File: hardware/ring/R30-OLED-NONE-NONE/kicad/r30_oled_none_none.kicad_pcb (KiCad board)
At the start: 2 copper layers, 43 x 18 mm, 28 parts, among them J1 off-board USB service pads, Q1 VBUS service jumper, SW1 5mm 200gf dome, U1 ESP32-C3-MINI-1-N4, U2 PAW3204DB-TJ3L, U3 TP4054, U4 RT9080-33GJ5

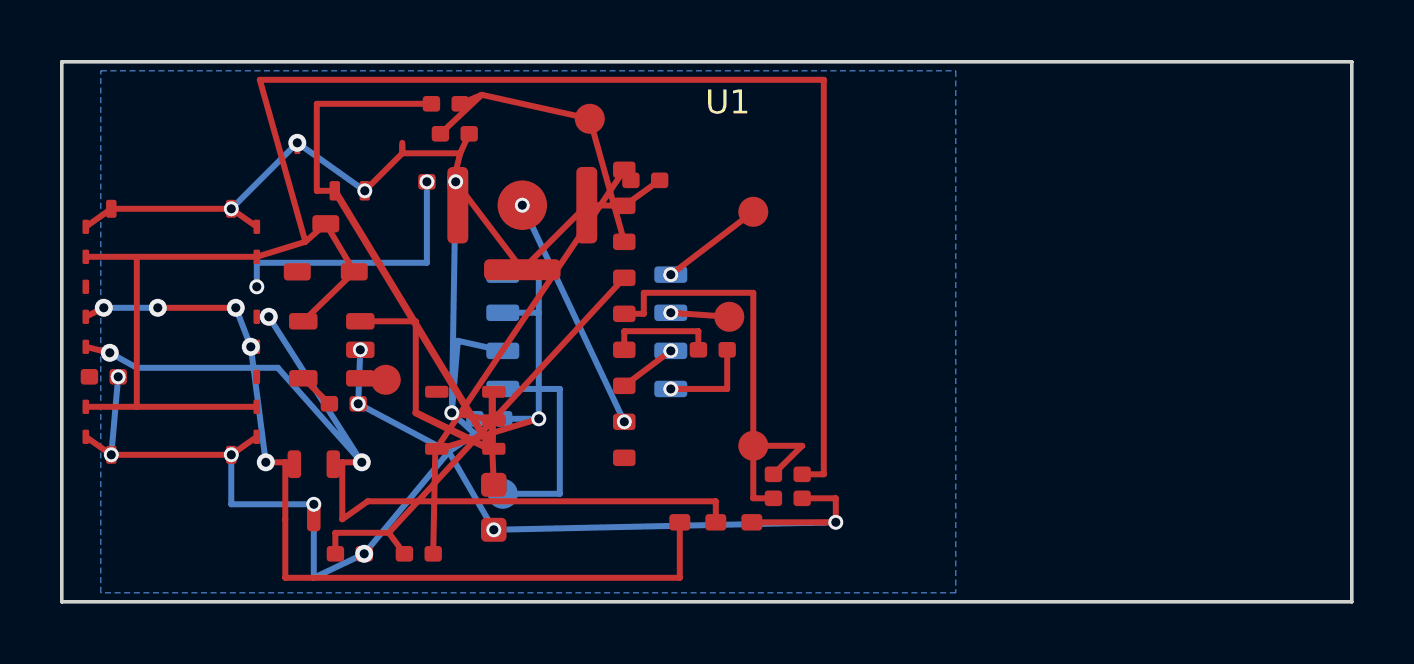
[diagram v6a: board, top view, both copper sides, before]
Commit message: fix(r30): nudge mcu decoupler clearance
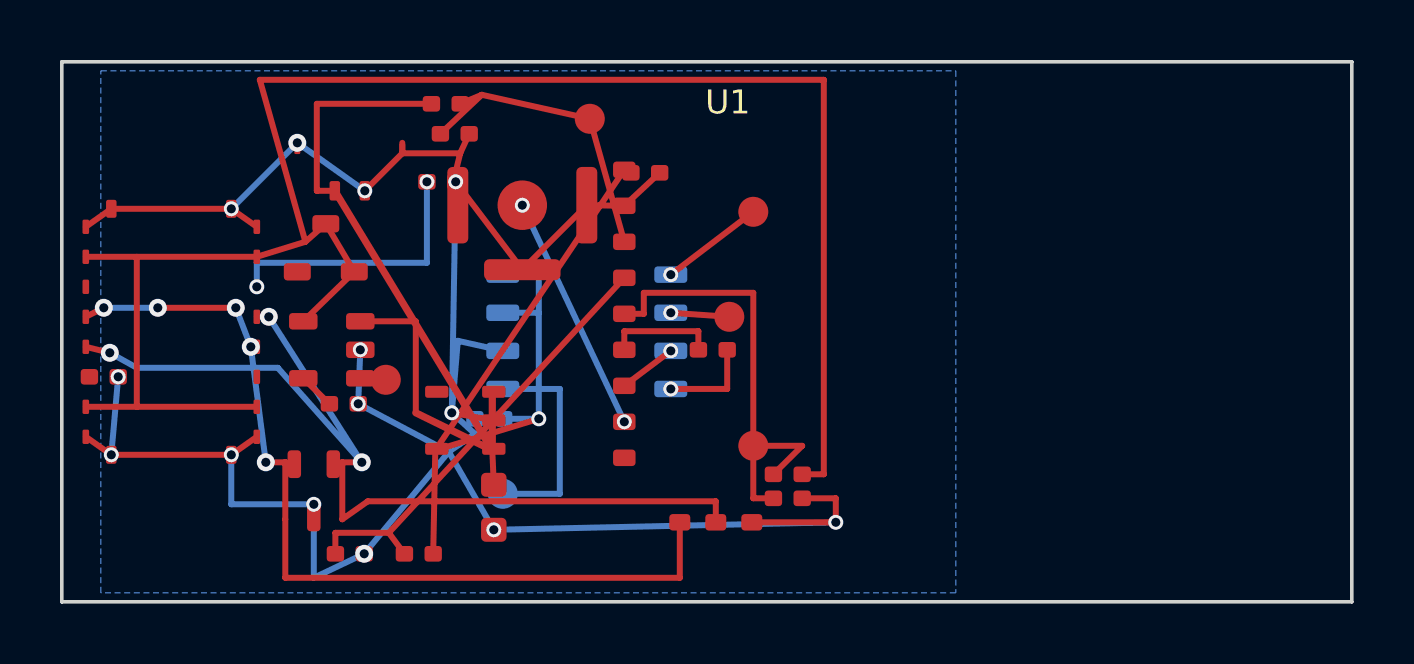
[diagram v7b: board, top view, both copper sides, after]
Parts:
- moved C1A 0.25 mm to (118.5, 94.7)
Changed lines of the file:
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@@
   (footprint "Capacitor_SMD:C_0402_1005Metric"
     (layer "F.Cu")
-    (at 118.450 94.950 0)
+    (at 118.450 94.700 0)
     (property "Reference" "C1A" (at 0 -1.05 0) (layer "F.Fab") (effects (font (size 0.6 0.6) (thickness 0.09))))
     (property "Value" "100nF MCU" (at 0 1.05 0) (layer "F.Fab") (effects (font (size 0.55 0.55) (thickness 0.08))))
@@
   (segment (start 113.350 103.950) (end 113.350 102.050) (width 0.24) (layer "F.Cu") (net 4))
   (segment (start 111.450 103.950) (end 117.750 94.600) (width 0.20) (layer "F.Cu") (net 5))
-  (segment (start 117.750 94.600) (end 117.970 94.950) (width 0.24) (layer "F.Cu") (net 5))
+  (segment (start 117.750 94.600) (end 117.970 94.700) (width 0.24) (layer "F.Cu") (net 5))
   (segment (start 111.450 103.950) (end 111.380 107.400) (width 0.20) (layer "F.Cu") (net 5))
   (segment (start 111.450 103.950) (end 114.900 102.900) (width 0.20) (layer "F.Cu") (net 5))
@@
   (segment (start 124.800 105.550) (end 124.800 106.350) (width 0.20) (layer "F.Cu") (net 1))
   (segment (start 124.800 106.350) (end 122.000 106.350) (width 0.20) (layer "F.Cu") (net 1))
-  (segment (start 118.930 94.950) (end 117.750 95.800) (width 0.20) (layer "F.Cu") (net 1))
+  (segment (start 118.930 94.700) (end 117.750 95.800) (width 0.20) (layer "F.Cu") (net 1))
   (segment (start 116.500 95.780) (end 117.750 95.800) (width 0.20) (layer "F.Cu") (net 1))
   (segment (start 108.120 107.400) (end 108.120 106.700) (width 0.20) (layer "F.Cu") (net 9))

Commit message: fix(r30): reroute vbat sense support corridor
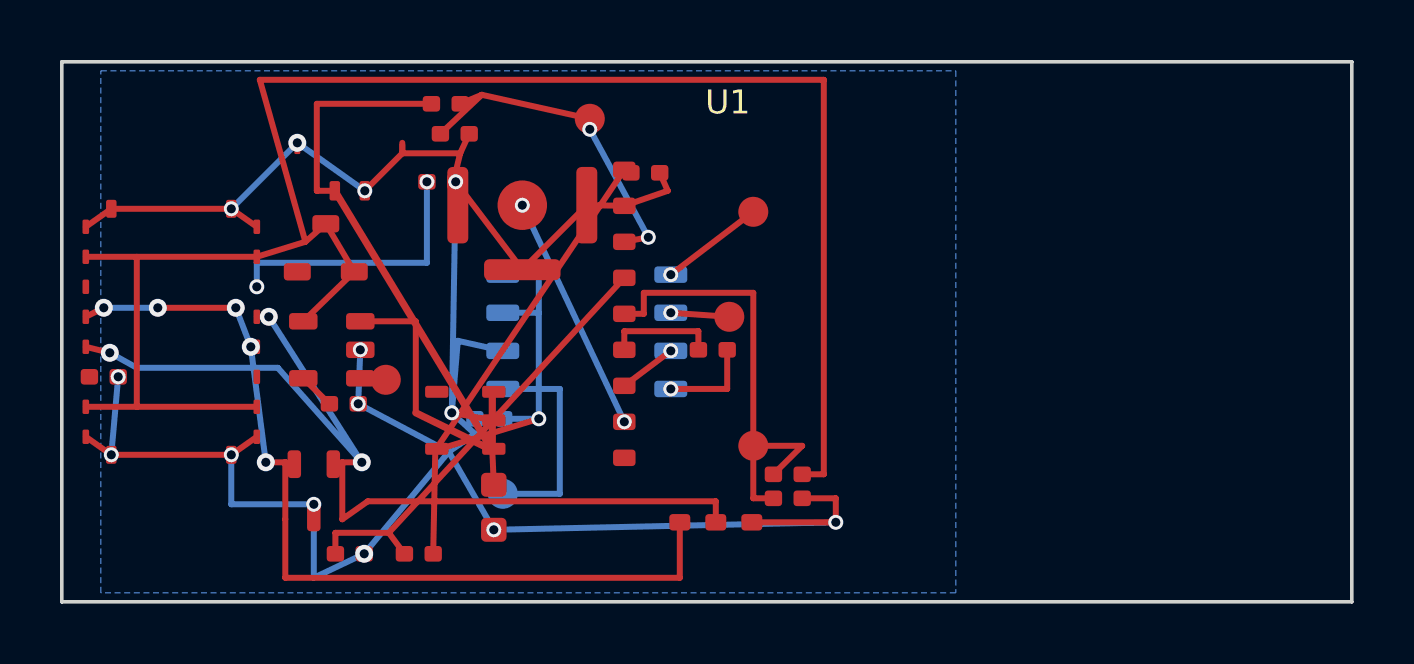
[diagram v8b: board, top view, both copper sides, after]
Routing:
- net VBAT_SENSE: track 10.6 -> 11.6 mm, vias 0 -> 2
- net GND: track 89.1 -> 89.7 mm
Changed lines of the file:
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@@
   (segment (start 124.800 105.550) (end 124.800 106.350) (width 0.20) (layer "F.Cu") (net 1))
   (segment (start 124.800 106.350) (end 122.000 106.350) (width 0.20) (layer "F.Cu") (net 1))
-  (segment (start 118.930 94.700) (end 117.750 95.800) (width 0.20) (layer "F.Cu") (net 1))
+  (segment (start 118.930 94.700) (end 119.200 95.300) (width 0.20) (layer "F.Cu") (net 1))
+  (segment (start 119.200 95.300) (end 117.750 95.800) (width 0.20) (layer "F.Cu") (net 1))
   (segment (start 116.500 95.780) (end 117.750 95.800) (width 0.20) (layer "F.Cu") (net 1))
   (segment (start 108.120 107.400) (end 108.120 106.700) (width 0.20) (layer "F.Cu") (net 9))
@@
   (segment (start 111.620 93.400) (end 113.000 92.100) (width 0.20) (layer "F.Cu") (net 21))
   (segment (start 113.000 92.100) (end 116.600 92.900) (width 0.20) (layer "F.Cu") (net 21))
-  (segment (start 116.600 92.900) (end 117.750 97.000) (width 0.20) (layer "F.Cu") (net 21))
+  (segment (start 116.600 92.900) (end 116.600 93.250) (width 0.20) (layer "F.Cu") (net 21))
+  (via (at 116.600 93.250) (size 0.50) (drill 0.30) (layers "F.Cu" "B.Cu") (net 21))
+  (segment (start 116.600 93.250) (end 118.550 96.850) (width 0.20) (layer "B.Cu") (net 21))
+  (via (at 118.550 96.850) (size 0.50) (drill 0.30) (layers "F.Cu" "B.Cu") (net 21))
+  (segment (start 118.550 96.850) (end 117.750 97.000) (width 0.20) (layer "F.Cu") (net 21))
   (segment (start 117.750 99.400) (end 118.400 99.400) (width 0.20) (layer "F.Cu") (net 22))
   (segment (start 118.400 99.400) (end 118.400 98.700) (width 0.20) (layer "F.Cu") (net 22))
